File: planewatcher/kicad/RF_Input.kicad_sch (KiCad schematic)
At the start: 13 parts, among them U2 AP22653AW6-7

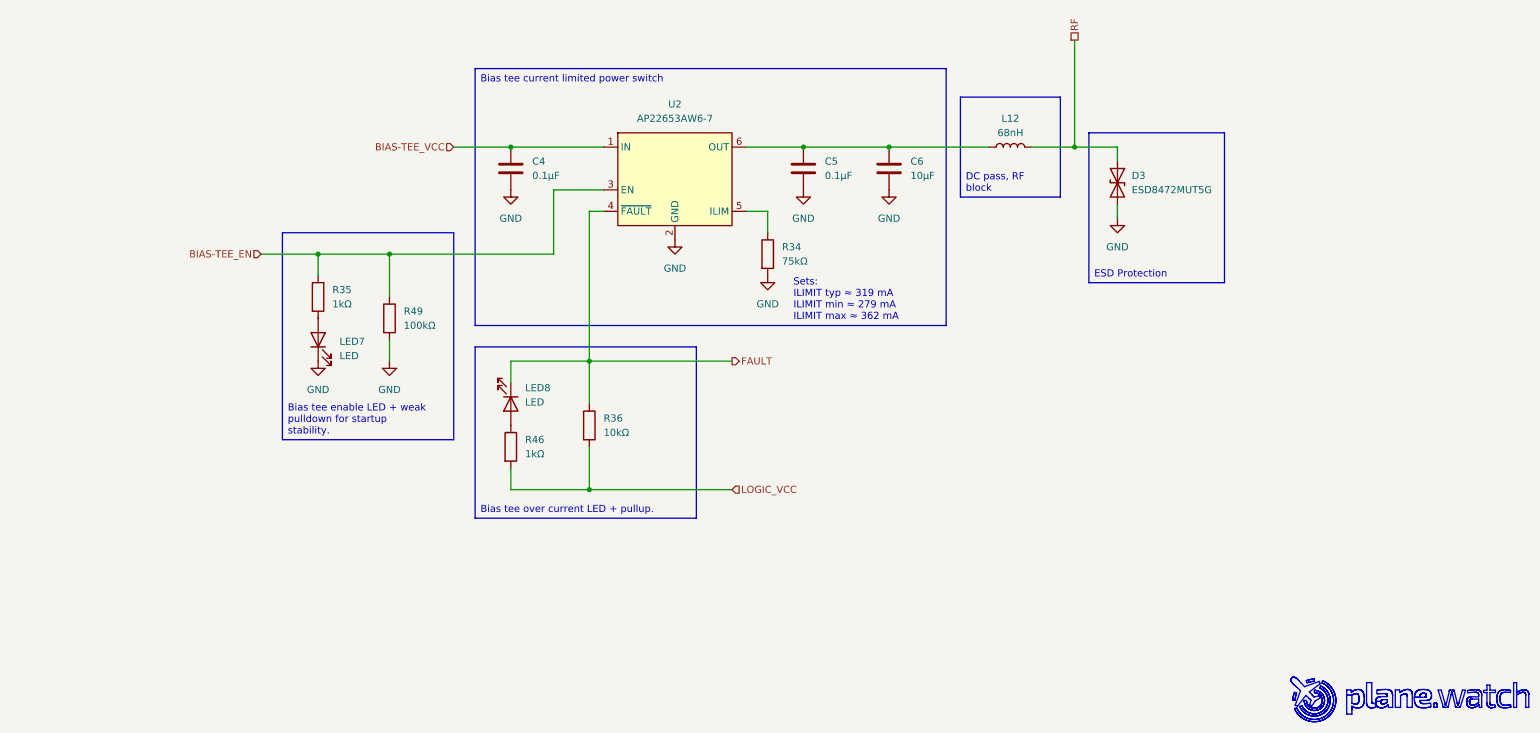
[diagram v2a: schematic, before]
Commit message: Add optional 2-section input LC matching/filter network
Default: series 0R, shunts DNP.
Populate after VNA/S11 testing to compensate ESD/bias-tee/LNA input parasitics.
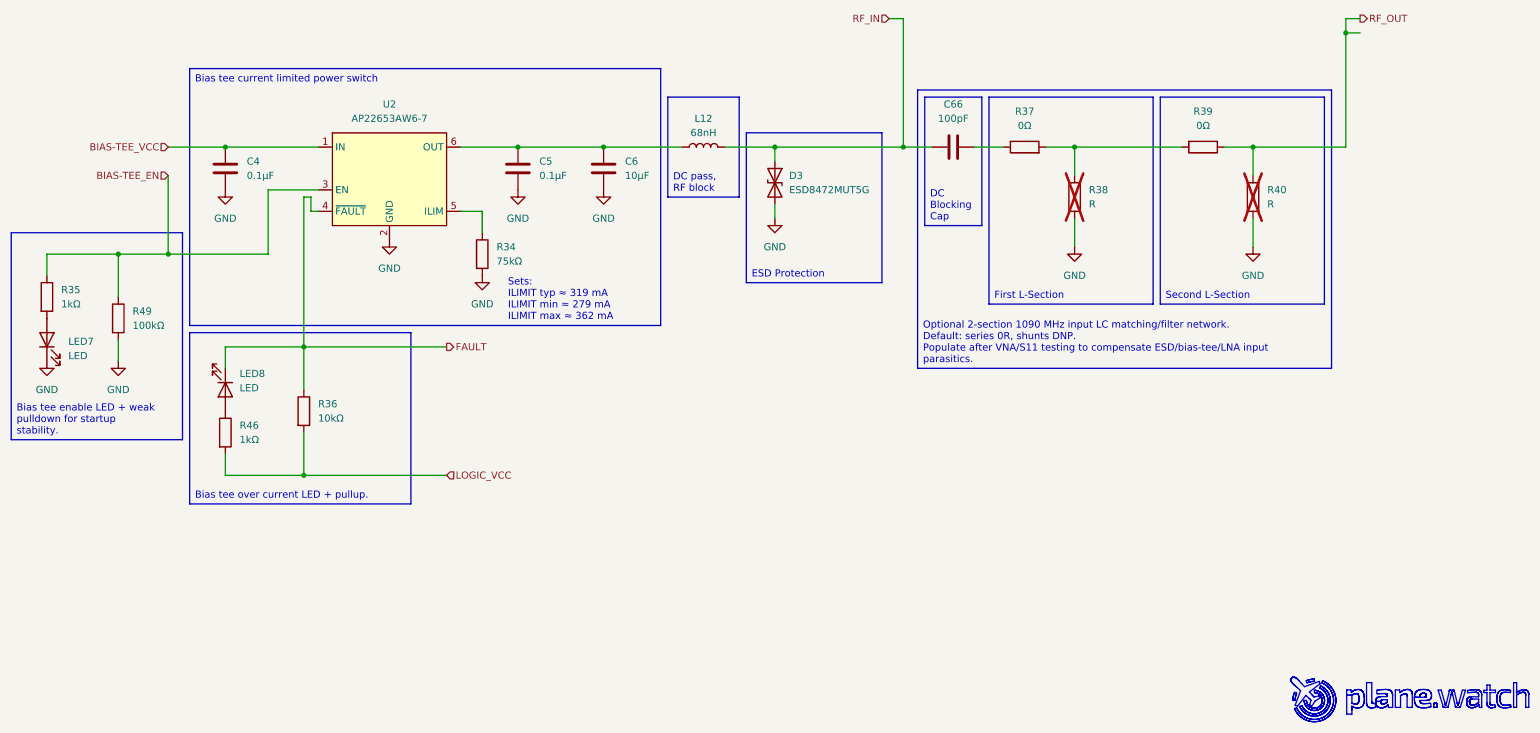
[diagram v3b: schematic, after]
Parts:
- added C66: 100pF, Capacitor_SMD:C_0402_1005Metric, symbol Device:C
- added R37, R39: 0Ω, Resistor_SMD:R_0402_1005Metric, symbol Device:R
- added R38, R40: R, Resistor_SMD:R_0402_1005Metric, symbol Device:R
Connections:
- net GND: now also R38.1, R40.2
- net RF renamed RF_IN
- net RF_IN: now also C66.2
- new net: C66.1, R37.1
- new net: R37.2, R38.2, R39.2
- new net RF_OUT: R39.1, R40.1
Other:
- moved on the sheet: C4, C5, C6, D3, L12, LED7, LED8, R34, R35, R36, R46, R49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

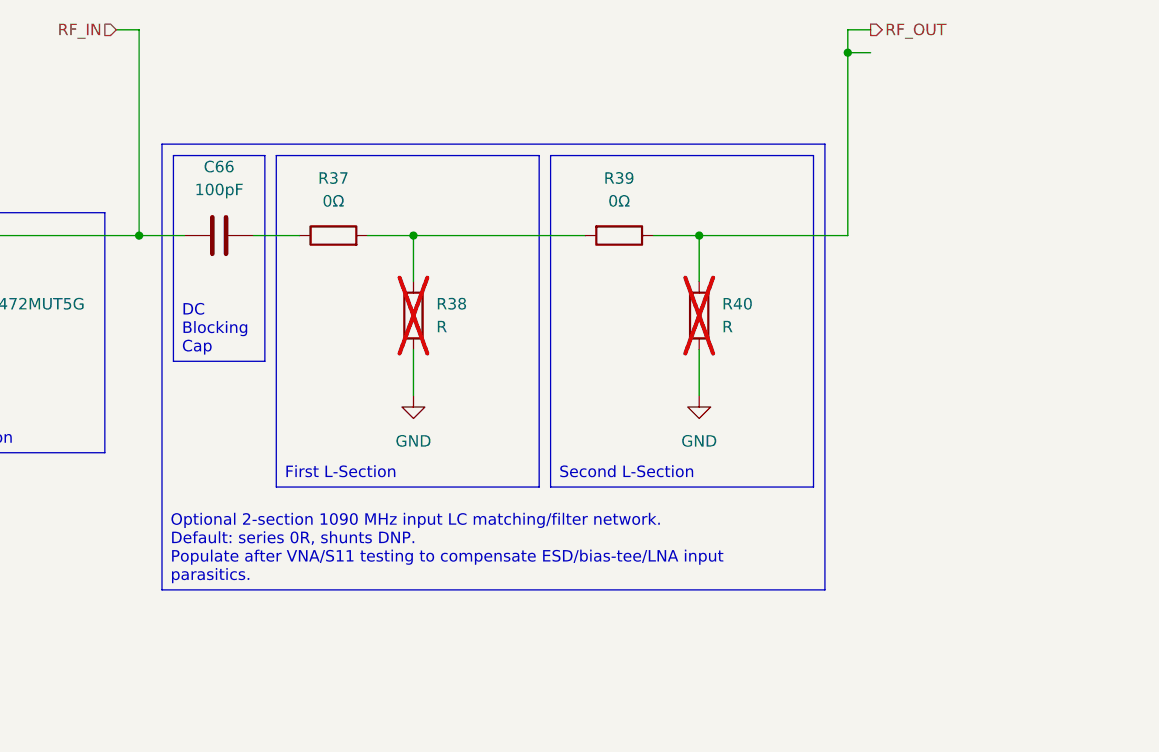
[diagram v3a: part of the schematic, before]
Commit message: Add RF frontend tuning footprints
Add DNP RF tuning footprints around the input match, SAW filter ports, and
log detector input path. Update schematic annotations for VNA-populated C/L/R
matching options, mark AD8138 feedback caps as optional, and update the PCB
layout for the new RF frontend tuning network.
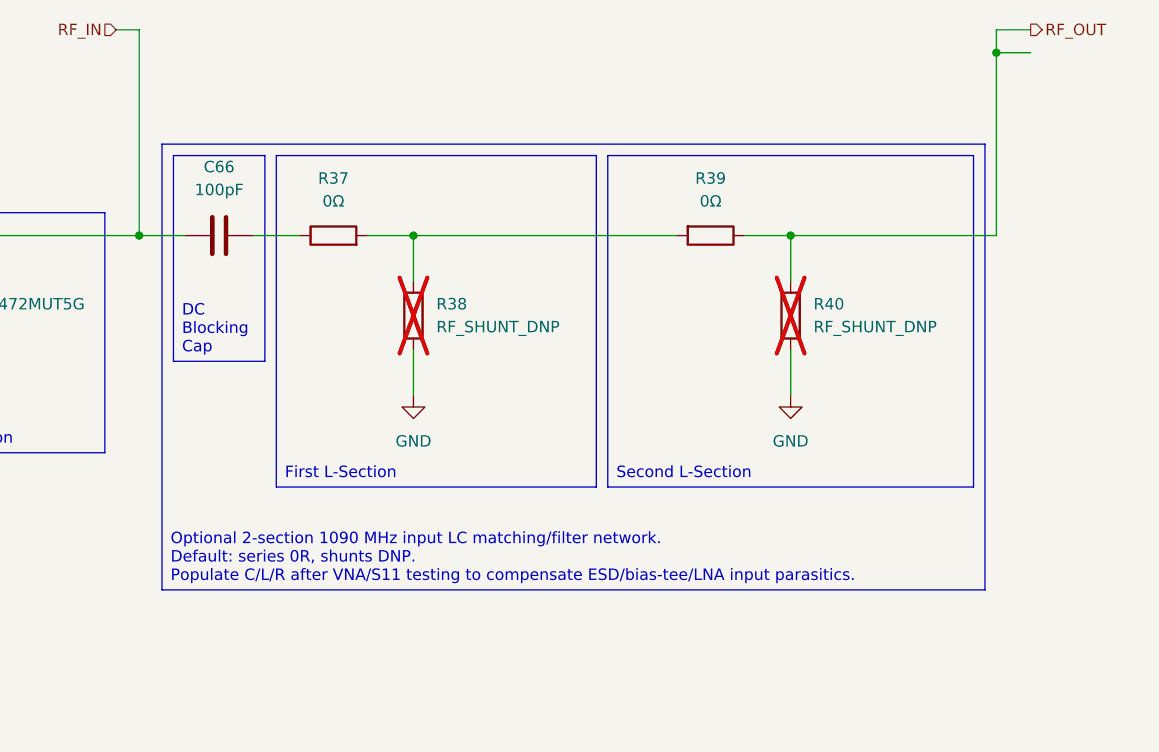
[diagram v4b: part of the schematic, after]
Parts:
- C66: Purpose RF bypass/matching capacitor in the 1090MHz LNA signal and 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 -> Bias tee DC blocking cap before matching network
- R37: MPN (none) -> ERJ-2GE0R00X; Manufacturer (none) -> Panasonic Industry; Package (none) -> 0402 (1005 Metric); Purpose (none) -> Series element in first L-Section. Populate C/L/R after VNA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; lcsc_id (none) -> C242160
- R38: value R -> RF_SHUNT_DNP; Purpose (none) -> Shunt element in first L-Section. Populate C/L/R after VNA/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
- R39: MPN (none) -> ERJ-2GE0R00X; Manufacturer (none) -> Panasonic Industry; Package (none) -> 0402 (1005 Metric); Purpose (none) -> Series element in second L-Section. Populate C/L/R after VN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; lcsc_id (none) -> C242160
- R40: value R -> RF_SHUNT_DNP; Purpose (none) -> Shunt element in second L-Section. Populate C/L/R after VNA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
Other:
- moved on the sheet: R39, R40

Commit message: Update land pattern for ESD diodes to match mfr datasheet
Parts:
- D3: footprint Diode_SMD:D_0201_0603Metric -> planewatcher:ESD8472
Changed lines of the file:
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@@
 			)
 		)
-		(property "Footprint" "Diode_SMD:D_0201_0603Metric"
+		(property "Footprint" "planewatcher:ESD8472"
 			(at 149.86 83.82 0)
 			(hide yes)
